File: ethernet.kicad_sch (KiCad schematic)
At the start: 62 parts, among them J6 Bus_RJ45_5-2337992-8, U15 KSZ9031RNXCA, Y2 Resonator_25MHz_ABM8G

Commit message: Finish schematic cleanup
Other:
- moved on the sheet: C134, C135, C136, C137, C138, C139, C140, C141, C142, C143, C144, C145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

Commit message: Clean schematic DRC
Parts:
- J6: VSD_Class (none) -> Ethernet
- U15: Manufacturer Microchip -> Microchip Technology
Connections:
- net at U15.13 (NC): no longer U15.47 (NC)

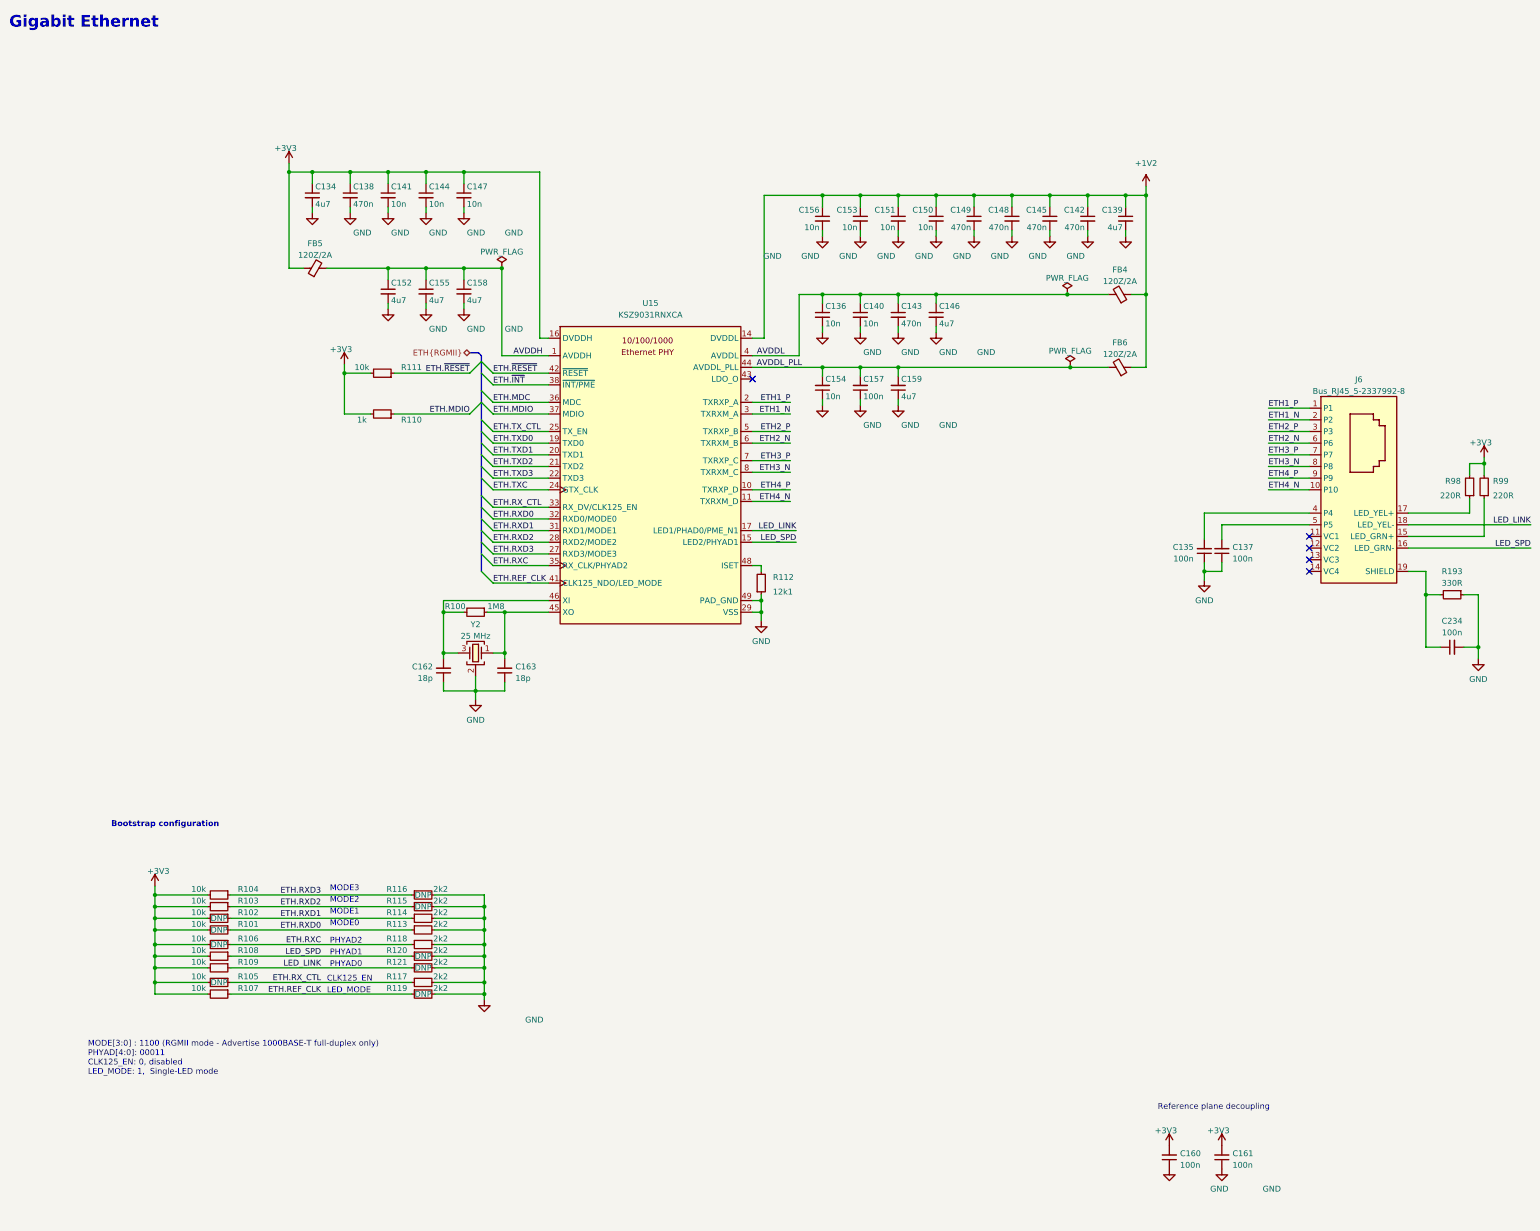
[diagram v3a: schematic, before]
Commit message: Add updated components to local library
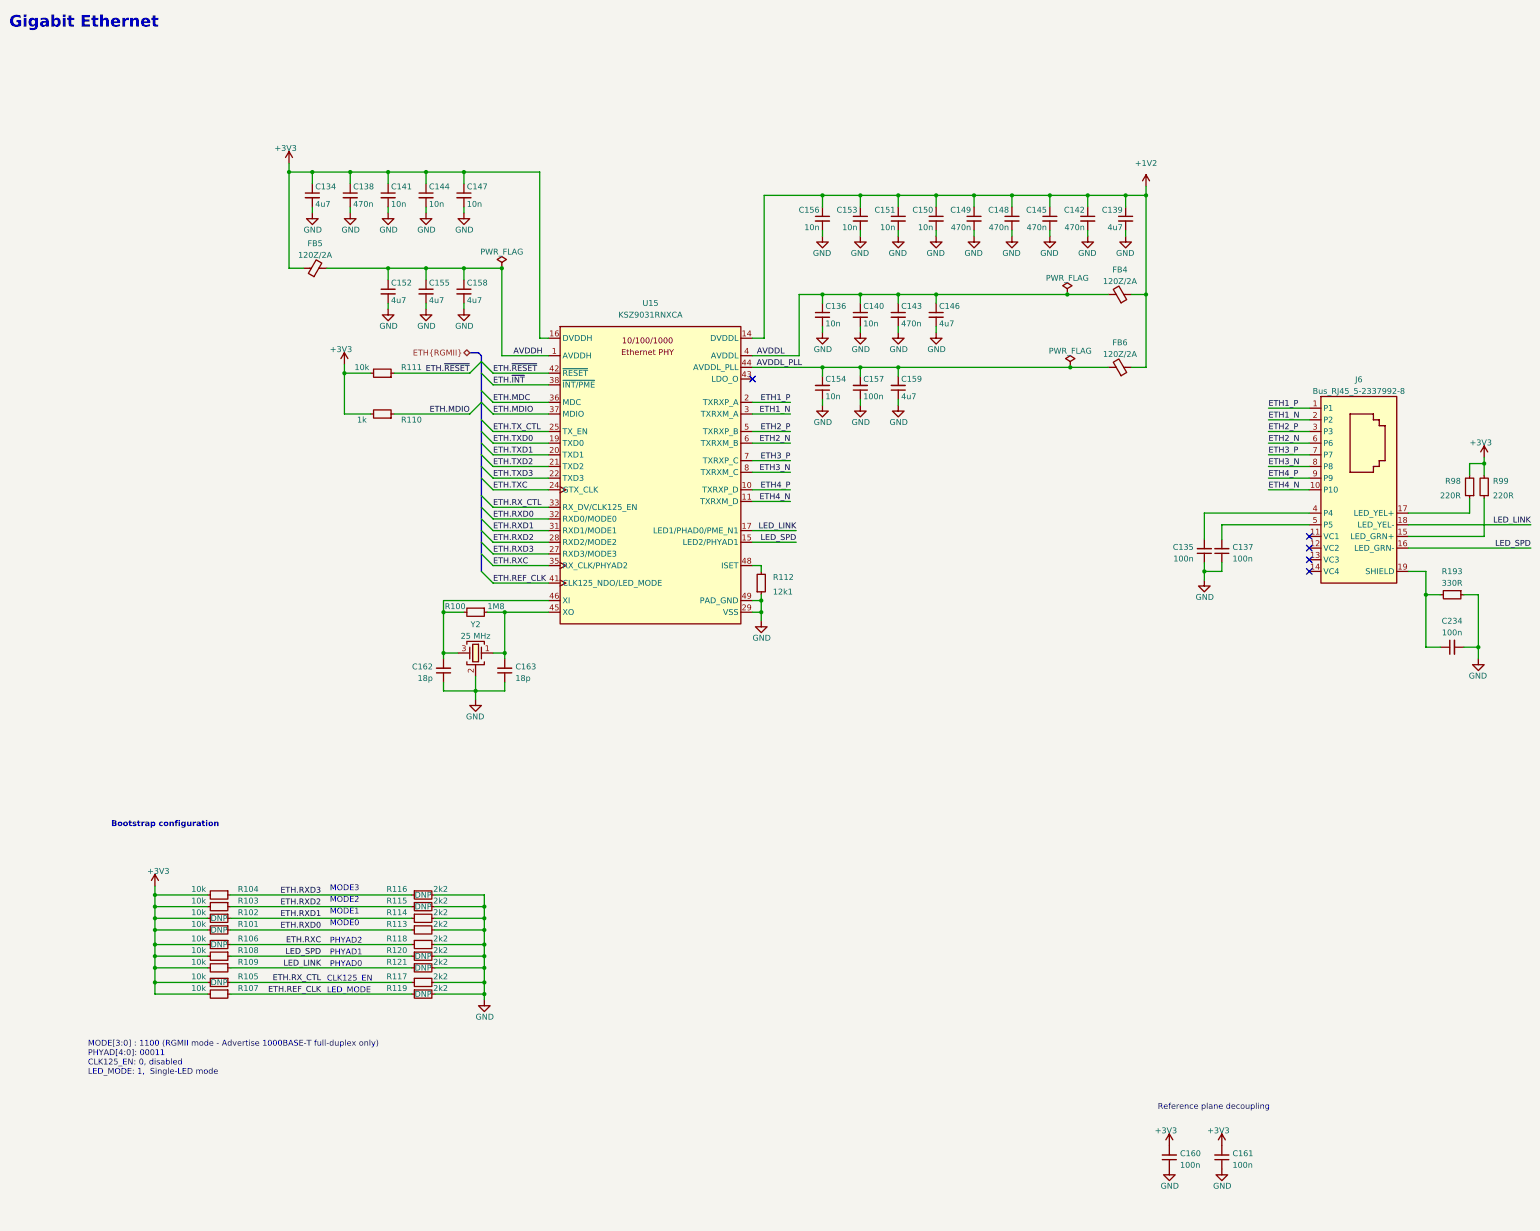
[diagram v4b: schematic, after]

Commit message: [#57478] ohp release
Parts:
- removed J6: Bus_RJ45_5-2337992-8, sodimm-ddr5-tester-footprints:RJ45_5-2337992-8_Horizontal, symbol sodimm-ddr5-tester:Bus_RJ45_5-2337992-8
- added J6: Bus_RJ45_5-2337992-8, antmicro-footprints:RJ45_X-2337992-8_Horizontal, symbol antmicroModularConnectorsJacksWithMagnetics:Bus_RJ45_5-2337992-8
- C134, C139, C146, C152, C155, C158, C159: footprint sodimm-ddr5-tester-footprints:C_0402_1005Metric -> antmicro-footprints:C_0402_1005Metric; symbol sodimm-ddr5-tester:C_4u7_0402 -> antmicroCapacitors0402:C_4u7_0402
- C135, C137, C157, C160, C161, C234: footprint sodimm-ddr5-tester-footprints:C_0402_1005Metric -> antmicro-footprints:C_0402_1005Metric; symbol sodimm-ddr5-tester:C_100n_0402 -> antmicroCapacitors0402:C_100n_0402
- C136, C140, C141, C144, C147, C150, C151, C153, C154, C156: footprint sodimm-ddr5-tester-footprints:C_0402_1005Metric -> antmicro-footprints:C_0402_1005Metric; symbol sodimm-ddr5-tester:C_10n_0402 -> antmicroCapacitors0402:C_10n_0402
- C138, C142, C143, C145, C148, C149: footprint sodimm-ddr5-tester-footprints:C_0402_1005Metric -> antmicro-footprints:C_0402_1005Metric; symbol sodimm-ddr5-tester:C_470n_0402 -> antmicroCapacitors0402:C_470n_0402
- C162, C163: footprint sodimm-ddr5-tester-footprints:C_0402_1005Metric -> antmicro-footprints:C_0402_1005Metric; symbol sodimm-ddr5-tester:C_18p_0402 -> antmicroCapacitors0402:C_18p_0402
- FB4, FB5, FB6: footprint sodimm-ddr5-tester-footprints:FB_0603_1608Metric -> antmicro-footprints:FB_0603_1608Metric; symbol sodimm-ddr5-tester:FB_120Z_2A_Murata-BLM18PG_0603 -> antmicroFerriteBeadsandChips:FB_120Z_2A_Murata-BLM18PG_0603
- R100: footprint sodimm-ddr5-tester-footprints:R_0402_1005Metric -> antmicro-footprints:R_0402_1005Metric; symbol sodimm-ddr5-tester:R_1M8_0402 -> antmicroResistors0402:R_1M8_0402
- R101, R102, R105, R106: footprint sodimm-ddr5-tester-footprints:R_0402_1005Metric -> antmicro-footprints:R_0402_1005Metric; symbol sodimm-ddr5-tester:R_10k_0402 -> antmicroResistors0402:R_10k_0402; now not fitted; now left out of the parts list
- R103, R104, R107, R108, R109, R111: footprint sodimm-ddr5-tester-footprints:R_0402_1005Metric -> antmicro-footprints:R_0402_1005Metric; symbol sodimm-ddr5-tester:R_10k_0402 -> antmicroResistors0402:R_10k_0402
- R110: footprint sodimm-ddr5-tester-footprints:R_0402_1005Metric -> antmicro-footprints:R_0402_1005Metric; symbol sodimm-ddr5-tester:R_1k_0402 -> antmicroResistors0402:R_1k_0402
- R112: footprint sodimm-ddr5-tester-footprints:R_0402_1005Metric -> antmicro-footprints:R_0402_1005Metric; symbol sodimm-ddr5-tester:R_12k1_0402 -> antmicroResistors0402:R_12k1_0402
- R113, R114, R117, R118: footprint sodimm-ddr5-tester-footprints:R_0402_1005Metric -> antmicro-footprints:R_0402_1005Metric; symbol sodimm-ddr5-tester:R_2k2_0402 -> antmicroResistors0402:R_2k2_0402
- R115, R116, R119, R120, R121: footprint sodimm-ddr5-tester-footprints:R_0402_1005Metric -> antmicro-footprints:R_0402_1005Metric; symbol sodimm-ddr5-tester:R_2k2_0402 -> antmicroResistors0402:R_2k2_0402; now not fitted; now left out of the parts list
- R193: footprint sodimm-ddr5-tester-footprints:R_0402_1005Metric -> antmicro-footprints:R_0402_1005Metric; symbol sodimm-ddr5-tester:R_330R_0402 -> antmicroResistors0402:R_330R_0402
- R98, R99: footprint sodimm-ddr5-tester-footprints:R_0402_1005Metric -> antmicro-footprints:R_0402_1005Metric; symbol sodimm-ddr5-tester:R_220R_0402 -> antmicroResistors0402:R_220R_0402
- U15: footprint sodimm-ddr5-tester-footprints:QFN-48-1EP_7x7x0.9mm_P0.5mm_EP3.5x3.5mm -> antmicro-footprints:QFN-48-1EP_7x7x0.9mm_P0.5mm_EP3.5x3.5mm; symbol sodimm-ddr5-tester:KSZ9031RNXCA -> antmicroInterfaceControllers:KSZ9031RNXCA
- Y2: footprint sodimm-ddr5-tester-footprints:Oscillator_SMD_Geyer_KX-7-4Pin_3.2x2.5mm -> antmicro-footprints:Resonator_SMD_Abracon_ABM8G_3.2x2.5mm; symbol sodimm-ddr5-tester:Resonator_25MHz_ABM8G -> antmicroResonators:Resonator_25MHz_ABM8G
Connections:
- net ETH1_N: now also J6.2 (P2)
- net ETH1_P: now also J6.1 (P1)
- net ETH2_N: now also J6.6 (P6)
- net ETH2_P: now also J6.3 (P3)
- net ETH3_N: now also J6.8 (P8)
- net ETH3_P: now also J6.7 (P7)
- net ETH4_N: now also J6.10 (P10)
- net ETH4_P: now also J6.9 (P9)
- net LED_LINK: now also J6.18 (LED_YEL-)
- net LED_SPD: now also J6.16 (LED_GRN-)
- net at R98.1: now also J6.17 (LED_YEL+)
- net at R99.1: now also J6.15 (LED_GRN+)
- net at C135.2: now also J6.4 (P4)
- net at C137.2: now also J6.5 (P5)
- net at C234.1, R193.2: now also J6.19 (SHIELD), J6.20 (SHIELD)

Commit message: [#86301] Project refresh 81589
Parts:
- R101, R102, R105, R106, R115, R116, R119, R120, R121: DNP DNP -> (none)

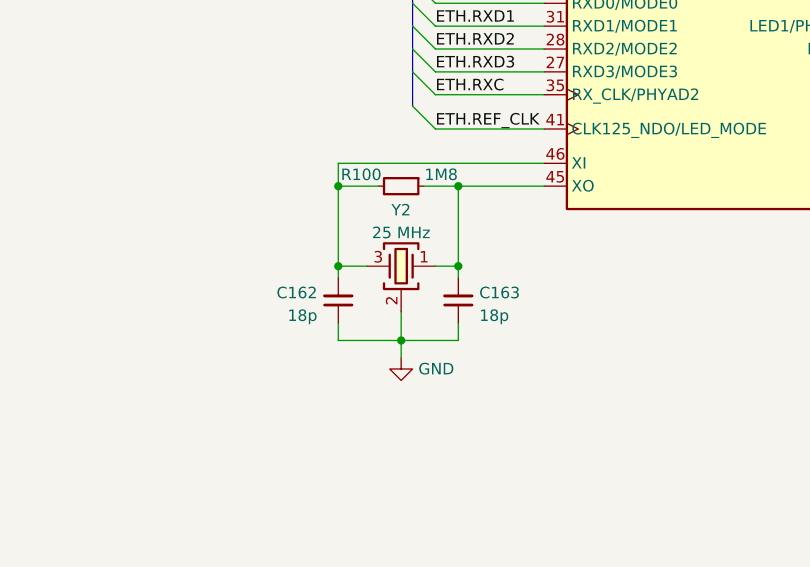
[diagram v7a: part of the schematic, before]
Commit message: [#87036] Update R100, bump revision to 1.3.0
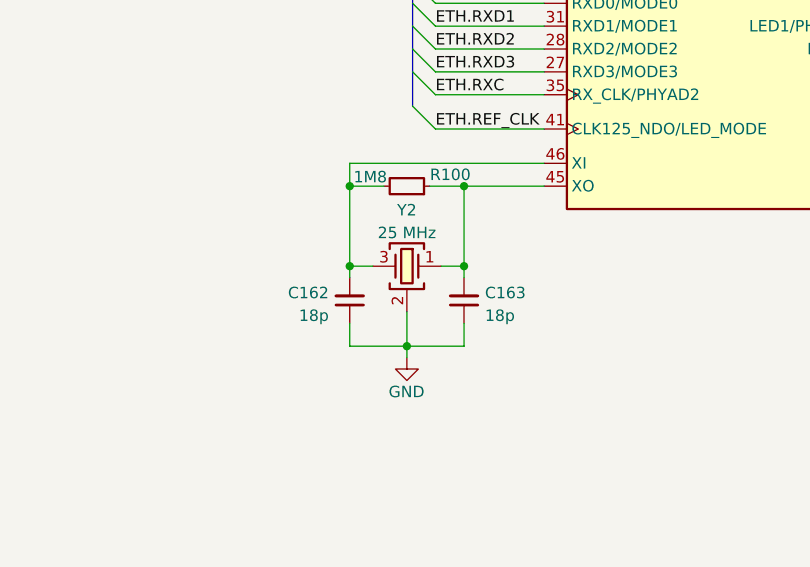
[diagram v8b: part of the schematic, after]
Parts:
- R100: MPN CR0402-FX-1804GLF -> RC0402FR-071M8L; Manufacturer Bourns -> YAGEO
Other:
- moved on the sheet: C162, C163, Y2
